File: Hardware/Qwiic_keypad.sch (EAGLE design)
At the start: 25 parts, among them J2 SMD, J3 PTH, J4 SMD, J6 AVR_SPI_PROG_3X2TESTPOINTS, U3 ATTINY84

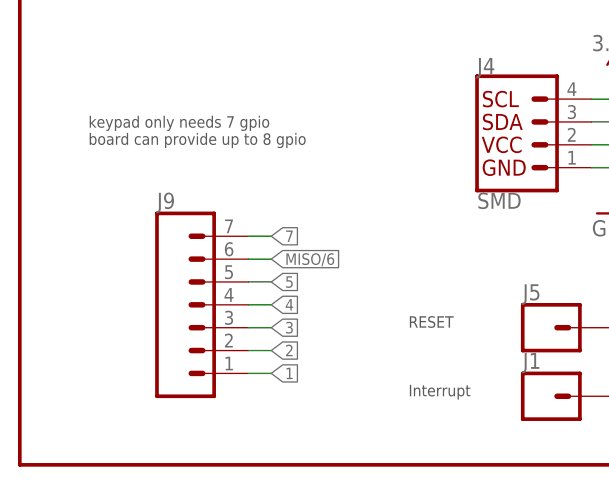
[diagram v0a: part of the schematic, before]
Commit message: changed header from 7 pin to 9 pin to accomidate extra pin on the keypad itself
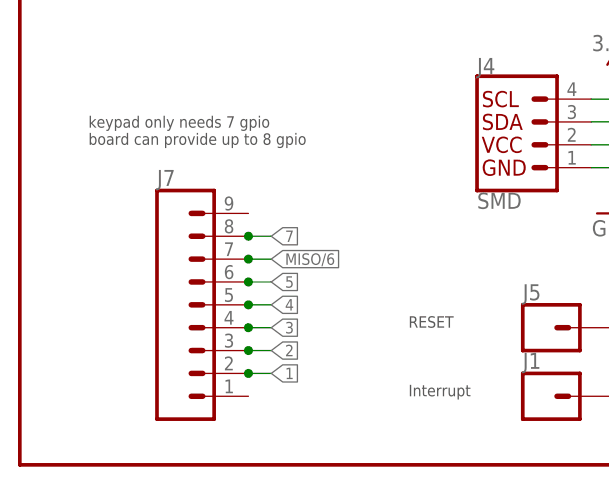
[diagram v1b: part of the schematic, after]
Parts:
- removed J9: (no value), SparkFun-Connectors:CONN_07NO_SILK
- added J7: (no value), SparkFun-Connectors:CONN_09NO_SILK
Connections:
- net 1: now also J7.2; no longer J9.1
- net 2: now also J7.3; no longer J9.2
- net 3: now also J7.4; no longer J9.3
- net 4: now also J7.5; no longer J9.4
- net 5: now also J7.6; no longer J9.5
- net 7: now also J7.8; no longer J9.7
- net MISO/6: now also J7.7; no longer J9.6
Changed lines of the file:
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@@
 <part name="JP1" library="SparkFun" deviceset="FIDUCIAL" device="UFIDUCIAL"/>
 <part name="JP3" library="SparkFun" deviceset="FIDUCIAL" device="UFIDUCIAL"/>
-<part name="J9" library="SparkFun-Connectors" deviceset="CONN_07" device="NO_SILK"/>
 <part name="J5" library="SparkFun-Connectors" deviceset="CONN_01" device="PTH_NO_SILK_YES_STOP"/>
+<part name="J7" library="SparkFun-Connectors" deviceset="CONN_09" device="NO_SILK"/>
 </parts>
 <sheets>
@@
 <instance part="JP1" gate="G$1" x="243.84" y="30.48"/>
 <instance part="JP3" gate="G$1" x="243.84" y="27.94"/>
-<instance part="J9" gate="G$1" x="20.32" y="15.24" smashed="yes">
-<attribute name="VALUE" x="15.24" y="5.334" size="1.778" layer="96" font="vector"/>
-<attribute name="NAME" x="15.24" y="28.448" size="1.778" layer="95" font="vector"/>
-</instance>
 <instance part="J5" gate="G$1" x="58.42" y="15.24"/>
+<instance part="J7" gate="G$1" x="15.24" y="17.78"/>
 </instances>
 <busses>
@@
 <wire x1="25.4" y1="17.78" x2="27.94" y2="17.78" width="0.1524" layer="91"/>
 <label x="27.94" y="17.78" size="1.27" layer="95" xref="yes"/>
-<pinref part="J9" gate="G$1" pin="4"/>
+<pinref part="J7" gate="G$1" pin="5"/>
+<junction x="25.4" y="17.78"/>
 </segment>
 <segment>
@@
 <wire x1="25.4" y1="15.24" x2="27.94" y2="15.24" width="0.1524" layer="91"/>
 <label x="27.94" y="15.24" size="1.27" layer="95" xref="yes"/>
-<pinref part="J9" gate="G$1" pin="3"/>
+<pinref part="J7" gate="G$1" pin="4"/>
+<junction x="25.4" y="15.24"/>
 </segment>
 <segment>
@@
 <wire x1="25.4" y1="12.7" x2="27.94" y2="12.7" width="0.1524" layer="91"/>
 <label x="27.94" y="12.7" size="1.27" layer="95" xref="yes"/>
-<pinref part="J9" gate="G$1" pin="2"/>
+<pinref part="J7" gate="G$1" pin="3"/>
+<junction x="25.4" y="12.7"/>
 </segment>
 <segment>
@@
 <wire x1="25.4" y1="10.16" x2="27.94" y2="10.16" width="0.1524" layer="91"/>
 <label x="27.94" y="10.16" size="1.27" layer="95" xref="yes"/>
-<pinref part="J9" gate="G$1" pin="1"/>
+<pinref part="J7" gate="G$1" pin="2"/>
+<junction x="25.4" y="10.16"/>
 </segment>
 <segment>
@@
 <wire x1="25.4" y1="22.86" x2="27.94" y2="22.86" width="0.1524" layer="91"/>
 <label x="27.94" y="22.86" size="1.27" layer="95" xref="yes"/>
-<pinref part="J9" gate="G$1" pin="6"/>
+<pinref part="J7" gate="G$1" pin="7"/>
+<junction x="25.4" y="22.86"/>
 </segment>
 <segment>
@@
 <wire x1="25.4" y1="25.4" x2="27.94" y2="25.4" width="0.1524" layer="91"/>
 <label x="27.94" y="25.4" size="1.27" layer="95" xref="yes"/>
-<pinref part="J9" gate="G$1" pin="7"/>
+<pinref part="J7" gate="G$1" pin="8"/>
+<junction x="25.4" y="25.4"/>
 </segment>
 </net>
@@
 <wire x1="25.4" y1="20.32" x2="27.94" y2="20.32" width="0.1524" layer="91"/>
 <label x="27.94" y="20.32" size="1.27" layer="95" xref="yes"/>
-<pinref part="J9" gate="G$1" pin="5"/>
-</segment>
-</net>
+<pinref part="J7" gate="G$1" pin="6"/>
+<junction x="25.4" y="20.32"/>
+</segment>
+</net>

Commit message: Adding production ready firmware. Adding examples.
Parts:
- J2, J4: value SMD -> (none); device SparkX:I2C_STANDARDJS-1MM -> SparkFun-Connectors:QWIIC_CONNECTORJS-1MM
- J7: value (none) -> Keypad
- R1: device SparkFun-Resistors:2.2KOHM-0603-1/10W-1% -> SparkFun-Resistors:4.7KOHM-0603-1/10W-1%
- R3: device SparkFun-Resistors:2.2KOHM-0603-1/10W-1% -> SparkFun-Resistors:10KOHM-0603-1/10W-1%
- R6: device SparkFun-Resistors:2.2KOHM-0603-1/10W-1% -> SparkFun-Resistors:1KOHM-0603-1/10W-1%
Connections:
- net 3.3V: now also J2.2, J4.2; no longer J2.VCC, J4.VCC
- net GND: now also J2.1, J4.1; no longer J2.GND, J4.GND
- net SCL: now also J2.4, J4.4; no longer J2.SCL, J4.SCL
- net SDA: now also J2.3, J4.3; no longer J2.SDA, J4.SDA
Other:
- note added: "0"
- note added: "1"
- note added: "10"
- note added: "11"
- note added: "3"
- note added: "4"
- note added: "5"
- note added: "6"
- note added: "7"
- note added: "8"
- note added: "9"
- note added: "Arduino Pin:"
- note added: "I2C Address Selection Closed Jumper (Default): 0x4B Open Jumper: 0x4A"
- note removed: "Address Bit Selection Open Jumper: LSB Bit 0: 0x3C Close Jumper: LSB Bit 1: 0x3D Default Address: 0x3D"
- note removed: "Interrupt"
- note removed: "RESET"
- note removed: "keypad only needs 7 gpio board can provide up to 8 gpio"
- moved on the sheet: C4, D1, J1, J5, J7, JP5, R3, R6

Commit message: v2 update
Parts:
- removed J7: Keypad, SparkFun-Connectors:CONN_09NO_SILK
- removed JP5: JUMPER-SMT_2_NC_PASTE_NO-SILK, SparkFun-Jumpers:JUMPER-SMT_2_NC_PASTE_NO-SILK
- removed R4: 2.2k, SparkFun-Resistors:2.2KOHM-0603-1/10W-1%
- added H1, H2: STAND-OFF, SparkFun-Hardware:STAND-OFF
- added J8: (no value), SparkFun-Connectors:CONN_07NO_SILK
- added JP4: JUMPER-SMT_2_NO_SILK, SparkFun-Jumpers:JUMPER-SMT_2_NO_SILK
- R3: value 10k -> 2.2k; device SparkFun-Resistors:10KOHM-0603-1/10W-1% -> SparkFun-Resistors:2.2KOHM-0603-1/10W-1%
- SJ5: value JUMPER-SMT_3_2-NC_PASTE_SILK -> JUMPER-SMT_3_2-NC_TRACE_SILK; device SparkFun-Jumpers:JUMPER-SMT_3_2-NC_PASTE_SILK -> SparkFun-Jumpers:JUMPER-SMT_3_2-NC_TRACE_SILK
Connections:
- removed net SCL_PU1: R2.2, SJ5.1
- removed net SDA_PU1: R4.2, SJ5.3
- new net N$2: R2.2, SJ5.3
- new net N$3: R3.2, SJ5.1
- net 1: now also J8.1; no longer J7.2
- net 2: now also J8.2; no longer J7.3
- net 3: now also J8.3; no longer J7.4
- net 3.3V: no longer JP5.2
- net 4: now also J8.4; no longer J7.5
- net 5: now also J8.5; no longer J7.6
- net 7: now also J8.7; no longer J7.8
- net ADD1: now also JP4.2; no longer JP5.1, R3.2
- net GND: now also JP4.1; no longer R3.1
- net MISO/6: now also J8.6; no longer J7.7
- net SCL: now also R3.1; no longer R2.1
- net SDA: now also R2.1; no longer R4.1
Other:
- note added: "I2C Address Selection Open Jumper (Default): 0x4B Closed Jumper: 0x4A"
- note added: "X02"
- note removed: "I2C Address Selection Closed Jumper (Default): 0x4B Open Jumper: 0x4A"
- note removed: "X10"
- moved on the sheet: R2, R3
